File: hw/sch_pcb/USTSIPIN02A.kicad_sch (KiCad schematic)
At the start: 63 parts, among them M1 HOLE, M2 HOLE, M3 HOLE, M4 HOLE, M8 BMI-S-204-F, Q1 2SK2394-6, U1 OPA2314, U2 OPA2314, U3 ISL21080DIH312Z-TK 1V25, U4 TS7211, U5 TS5A4594

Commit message: Edit bom
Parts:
- C1, C21, C23, C4, C55, C56, C57, C58, C6, C7, C8, C9: value 10uF -> (none); footprint Capacitor_SMD:C_0603_1608Metric -> (none); UST_ID (none) -> 5c70984812875079b91f8bf5
- C10, C11, C12, C13, C14, C16, C2, C20, C59: value 100nF -> (none); footprint Capacitor_SMD:C_0603_1608Metric -> (none); UST_ID (none) -> 5c70984812875079b91f8bf2
- C15: value 3n3 -> (none); footprint Capacitor_SMD:C_0603_1608Metric -> (none); UST_ID (none) -> 628d0fc8dc56076e9a223574
- C17, C24, C3, C37: value 1uF -> (none); footprint Capacitor_SMD:C_0603_1608Metric -> (none); UST_ID (none) -> 5c70984812875079b91f8bc2
- C18: value 2n2 -> (none); footprint Capacitor_SMD:C_0603_1608Metric -> (none); UST_ID (none) -> 5c70984812875079b91f8bee
- C19: value 1nF/NP0 -> (none); footprint Capacitor_SMD:C_0805_2012Metric -> (none); UST_ID (none) -> 628d107bdc56076e9a2235a1
- C5: value 1pFNP0 251R15S1R0AV4E -> (none); footprint Capacitor_SMD:C_0805_2012Metric -> (none); UST_ID (none) -> 5c70984712875079b91f8b9f
- C53: value 10uF -> (none); footprint Resistor_SMD:R_0603_1608Metric -> (none); UST_ID (none) -> 5c70984812875079b91f8bf5
- D2: value S2744-09 -> (none); footprint Mlab_D:HAMAMATSU_S2744-09 -> (none); UST_ID (none) -> 628d118cdc56076e9a2235e4
- M1, M2, M3, M4: value HOLE -> (none); footprint Mlab_Mechanical:MountingHole_3mm -> (none)
- M8: value BMI-S-204-F -> (none); footprint RF_Shielding:Laird_Technologies_BMI-S-204-F_32.00x32.00mm -> (none); UST_ID (none) -> 5c72751c1287500b4e11301a
- Q1: value 2SK2394-6 -> (none); footprint Package_TO_SOT_SMD:SOT-23 -> (none); UST_ID (none) -> 628d134fdc56076e9a223625
- R1: value 10R -> (none); footprint Resistor_SMD:R_0603_1608Metric -> (none); UST_ID (none) -> 5c70984512875079b91f894f
- R10, R8: value 1k -> (none); footprint Resistor_SMD:R_0603_1608Metric -> (none); UST_ID (none) -> 5c70984512875079b91f895c
- R11, R14, R15, R16, R19, R22, R9: value 4k7 -> (none); footprint Resistor_SMD:R_0603_1608Metric -> (none); UST_ID (none) -> 5c70984512875079b91f8960
- R12, R7: value 10k -> (none); footprint Resistor_SMD:R_0603_1608Metric -> (none); UST_ID (none) -> 5c70984512875079b91f8962
- R13: value 2k2 -> (none); footprint Resistor_SMD:R_0603_1608Metric -> (none); UST_ID (none) -> 5c70984512875079b91f895e
- R2, R3, R4, R40, R5: value 470R -> (none); footprint Resistor_SMD:R_0603_1608Metric -> (none); UST_ID (none) -> 5c70984512875079b91f8959
- R39: value 100R -> (none); footprint Resistor_SMD:R_0603_1608Metric -> (none); UST_ID (none) -> 5c70984512875079b91f8956
- R41: value 0R -> (none); footprint Resistor_SMD:R_0603_1608Metric -> (none); UST_ID (none) -> 5c70984512875079b91f894e
- R6: value 10M -> (none); footprint Resistor_SMD:R_0603_1608Metric -> (none); UST_ID (none) -> 5c70984712875079b91f8b6d
- U1, U2: value OPA2314 -> (none); footprint Package_SO:SOIC-8_3.9x4.9mm_P1.27mm -> (none); UST_ID (none) -> 5c70984412875079b91f879b
- U3: value ISL21080DIH312Z-TK 1V25 -> (none); footprint Package_TO_SOT_SMD:SOT-23 -> (none); UST_ID (none) -> 5c70984712875079b91f8b7a
- U4: value TS7211 -> (none); footprint Package_TO_SOT_SMD:SOT-23-5_HandSoldering -> (none); UST_ID (none) -> 5c70984712875079b91f8b5b
- U5: value TS5A4594 -> (none); footprint Package_TO_SOT_SMD:SOT-23-5_HandSoldering -> (none); UST_ID (none) -> 5c70984612875079b91f8a0d

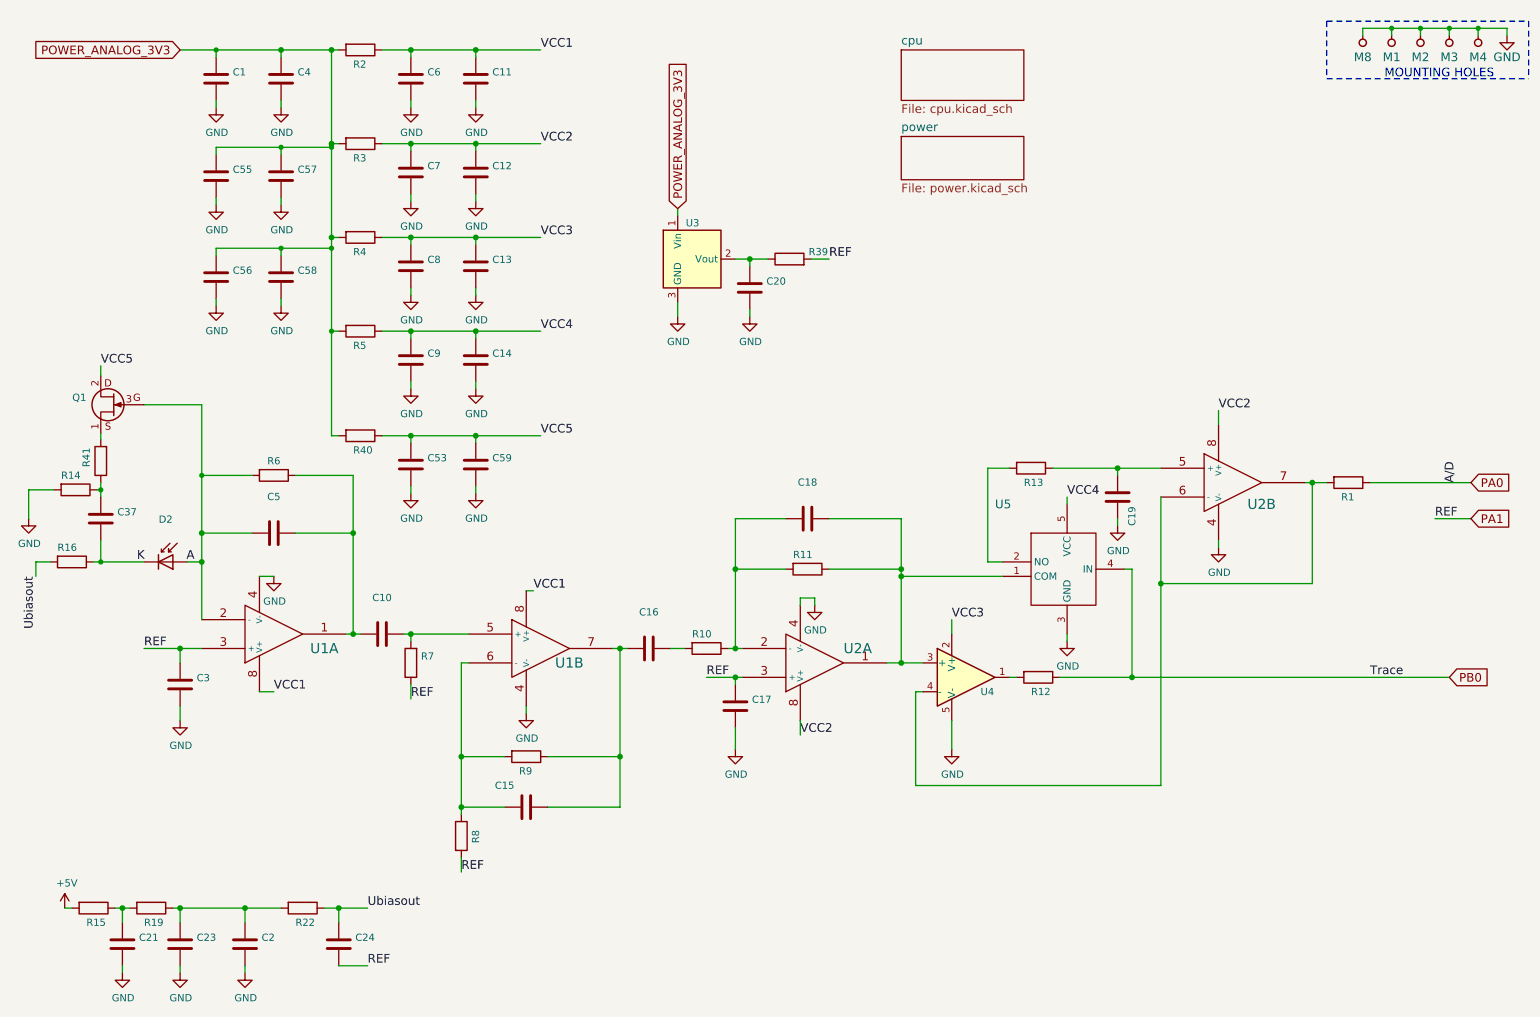
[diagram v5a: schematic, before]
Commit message: Cleaup old page layout. Title block update.
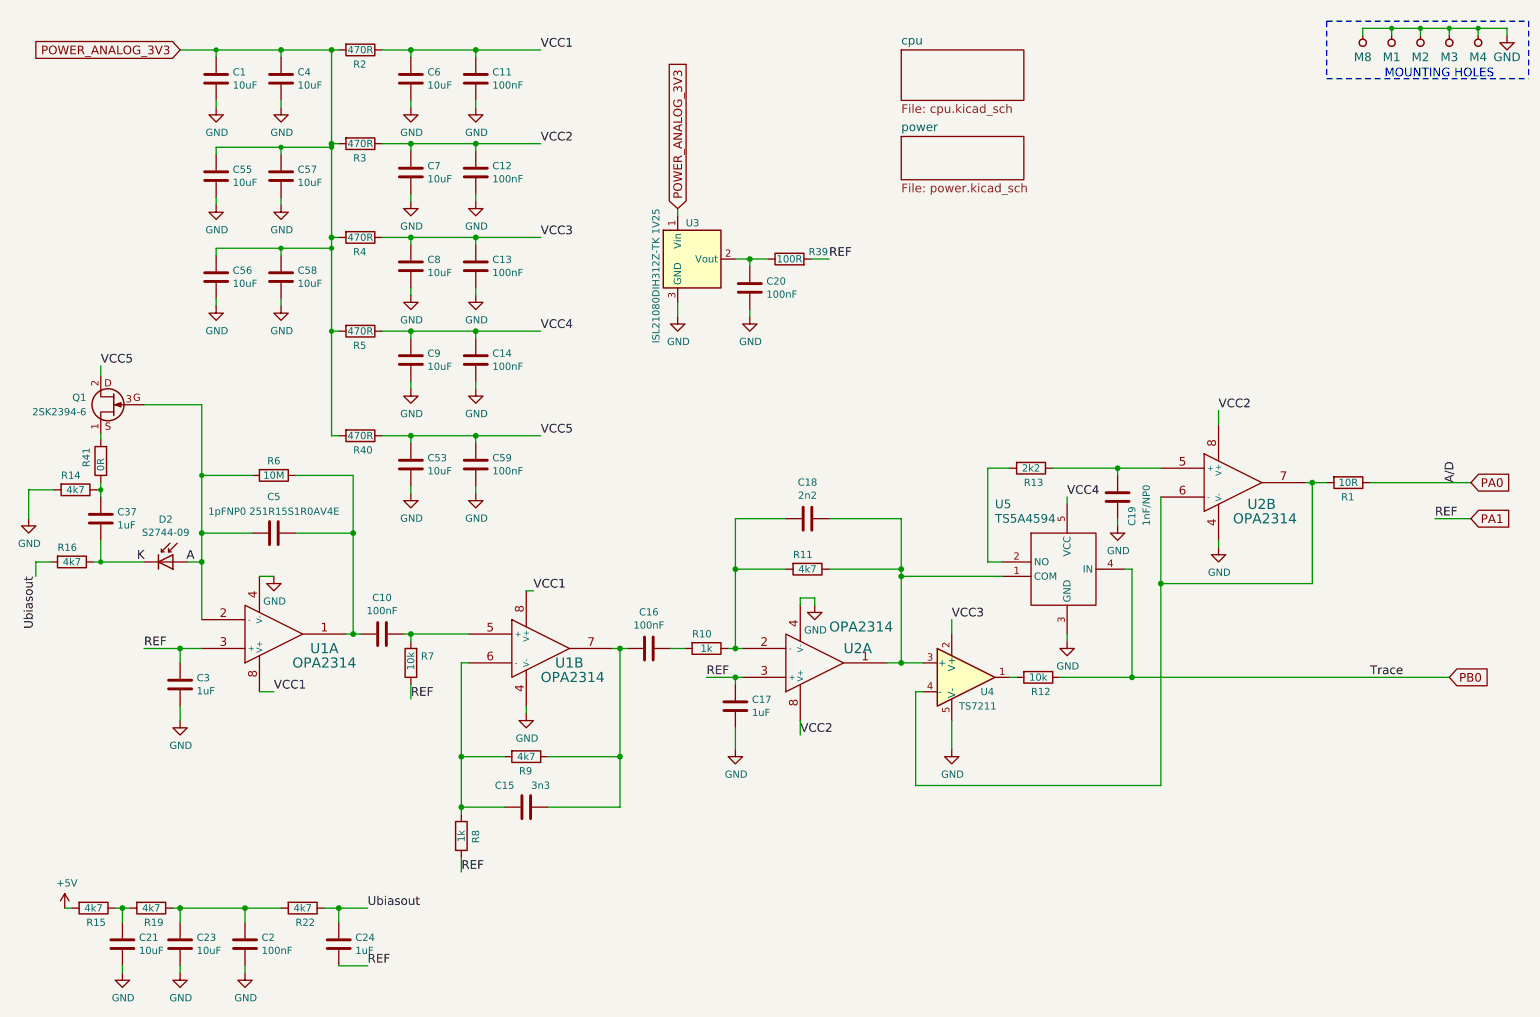
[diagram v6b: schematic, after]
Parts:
- C1, C21, C23, C4, C53, C55, C56, C57, C58, C6, C7, C8, C9: value (none) -> 10uF; footprint (none) -> Capacitor_SMD:C_0603_1608Metric
- C10, C11, C12, C13, C14, C16, C2, C20, C59: value (none) -> 100nF; footprint (none) -> Capacitor_SMD:C_0603_1608Metric
- C15: value (none) -> 3n3; footprint (none) -> Capacitor_SMD:C_0603_1608Metric
- C17, C24, C3, C37: value (none) -> 1uF; footprint (none) -> Capacitor_SMD:C_0603_1608Metric
- C18: value (none) -> 2n2; footprint (none) -> Capacitor_SMD:C_0603_1608Metric
- C19: value (none) -> 1nF/NP0; footprint (none) -> Capacitor_SMD:C_0805_2012Metric
- C5: value (none) -> 1pFNP0 251R15S1R0AV4E; footprint (none) -> Capacitor_SMD:C_0805_2012Metric
- D2: value (none) -> S2744-09; footprint (none) -> Mlab_D:HAMAMATSU_S2744-09
- M1, M2, M3, M4: value (none) -> HOLE; footprint (none) -> Mlab_Mechanical:MountingHole_3mm
- M8: value (none) -> BMI-S-204-F; footprint (none) -> RF_Shielding:Laird_Technologies_BMI-S-204-F_32.00x32.00mm
- Q1: value (none) -> 2SK2394-6; footprint (none) -> Package_TO_SOT_SMD:SOT-23
- R1: value (none) -> 10R; footprint (none) -> Resistor_SMD:R_0603_1608Metric
- R10, R8: value (none) -> 1k; footprint (none) -> Resistor_SMD:R_0603_1608Metric
- R11, R14, R15, R16, R19, R22, R9: value (none) -> 4k7; footprint (none) -> Resistor_SMD:R_0603_1608Metric
- R12, R7: value (none) -> 10k; footprint (none) -> Resistor_SMD:R_0603_1608Metric
- R13: value (none) -> 2k2; footprint (none) -> Resistor_SMD:R_0603_1608Metric
- R2, R3, R4, R40, R5: value (none) -> 470R; footprint (none) -> Resistor_SMD:R_0603_1608Metric
- R39: value (none) -> 100R; footprint (none) -> Resistor_SMD:R_0603_1608Metric
- R41: value (none) -> 0R; footprint (none) -> Resistor_SMD:R_0603_1608Metric
- R6: value (none) -> 10M; footprint (none) -> Resistor_SMD:R_0603_1608Metric
- U1, U2: value (none) -> OPA2314; footprint (none) -> Package_SO:SOIC-8_3.9x4.9mm_P1.27mm
- U3: value (none) -> ISL21080DIH312Z-TK 1V25; footprint (none) -> Package_TO_SOT_SMD:SOT-23
- U4: value (none) -> TS7211; footprint (none) -> Package_TO_SOT_SMD:SOT-23-5_HandSoldering
- U5: value (none) -> TS5A4594; footprint (none) -> Package_TO_SOT_SMD:SOT-23-5_HandSoldering

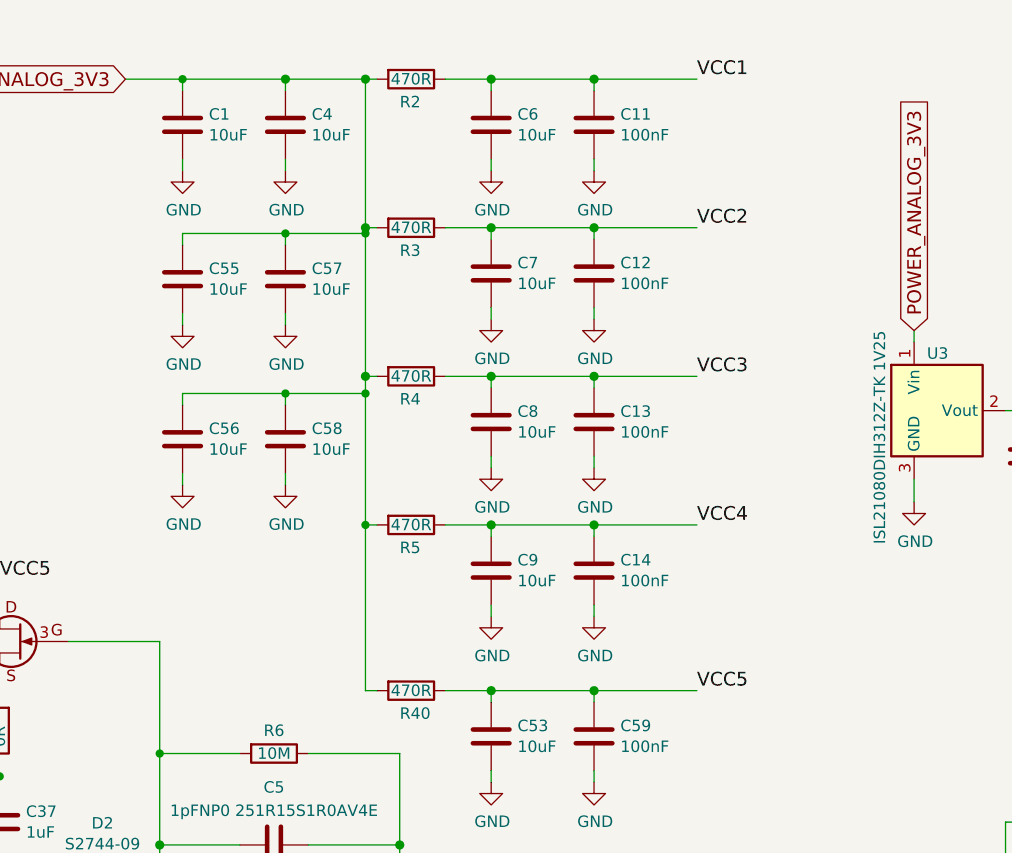
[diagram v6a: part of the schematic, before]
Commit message: Add power flags to make specific ERC issues as known.
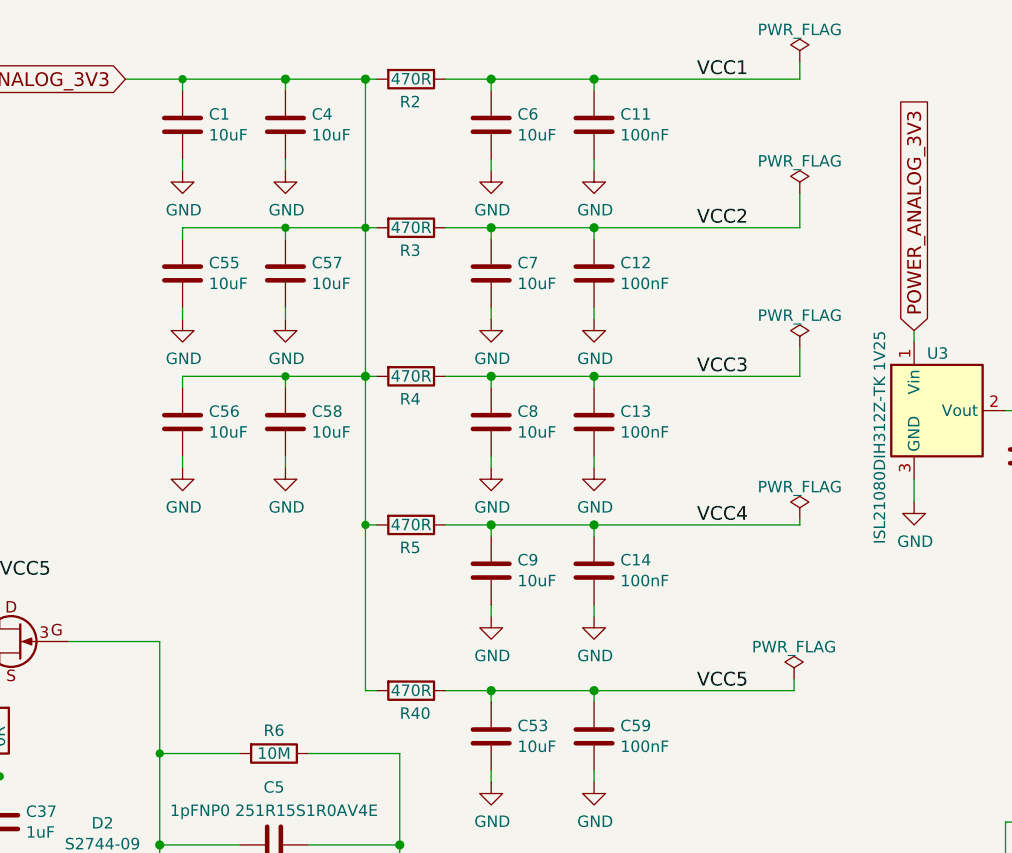
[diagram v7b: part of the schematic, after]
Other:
- moved on the sheet: C55, C56, C57, C58
